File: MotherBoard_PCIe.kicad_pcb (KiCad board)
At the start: 2 copper layers, 91 x 196 mm, 43 parts, among them J1 XT60-M, J10 Bus_mechaken_PCIexpress_x16_1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, J11 Conn_01x03, J12 Conn_01x03, J13 Conn_01x03, J2 XT60-F, J3 Conn_01x07, J4 Conn_01x07, J5 Bus_mechaken_PCIexpress_x16_1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, J6 Bus_mechaken_PCIexpress_x16_1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, J7 Bus_mechaken_PCIexpress_x16_1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, J8 Bus_mechaken_PCIexpress_x16_1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, J9 Bus_mechaken_PCIexpress_x16_1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, U1 NJM7812S

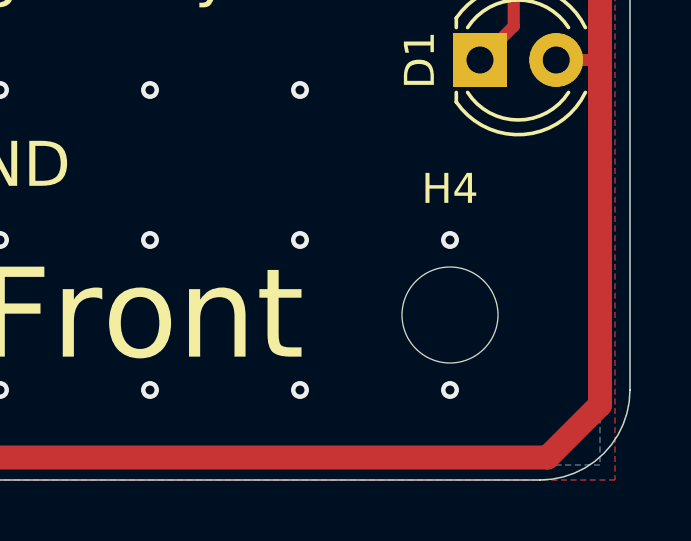
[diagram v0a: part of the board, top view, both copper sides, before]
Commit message: fix
H4にM3ねじを使ったらビアから導通しそうだったので修正
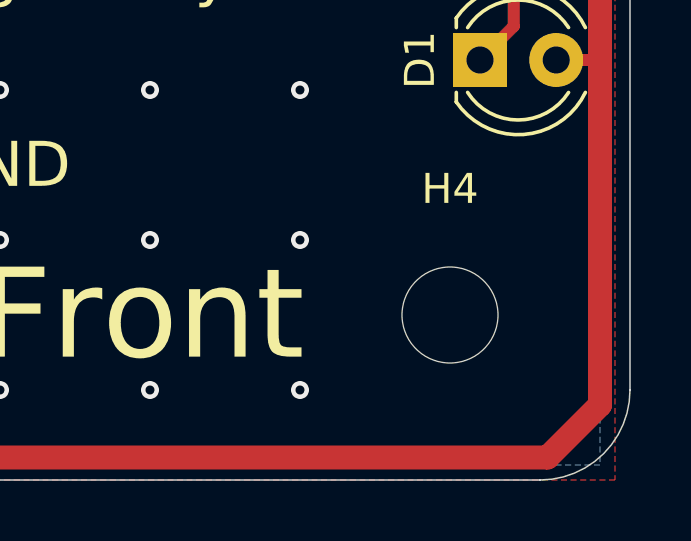
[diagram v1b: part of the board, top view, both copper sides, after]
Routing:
- net GNDPWR: vias 257 -> 255

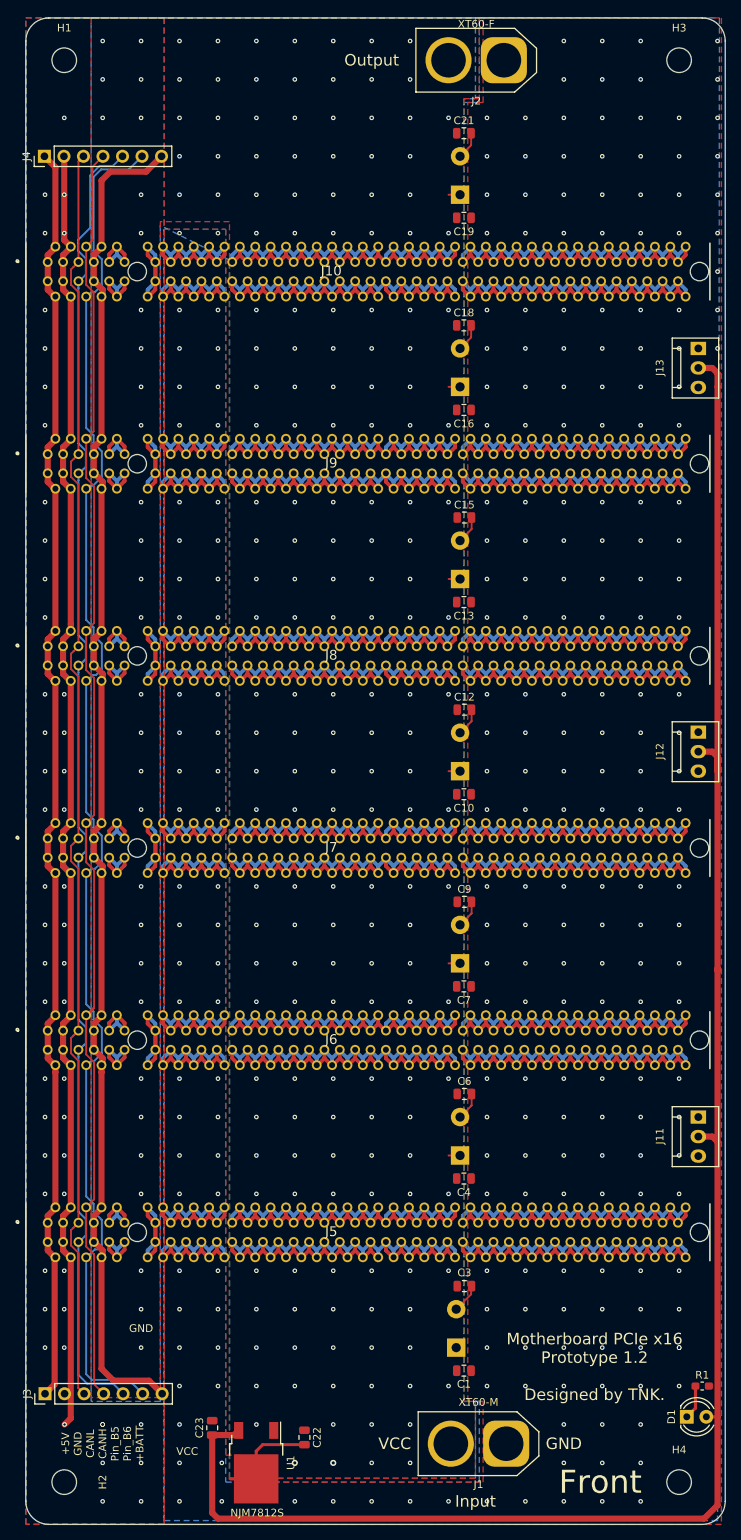
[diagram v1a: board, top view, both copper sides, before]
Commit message: change
シルク印刷の修正（githubのリンク等）
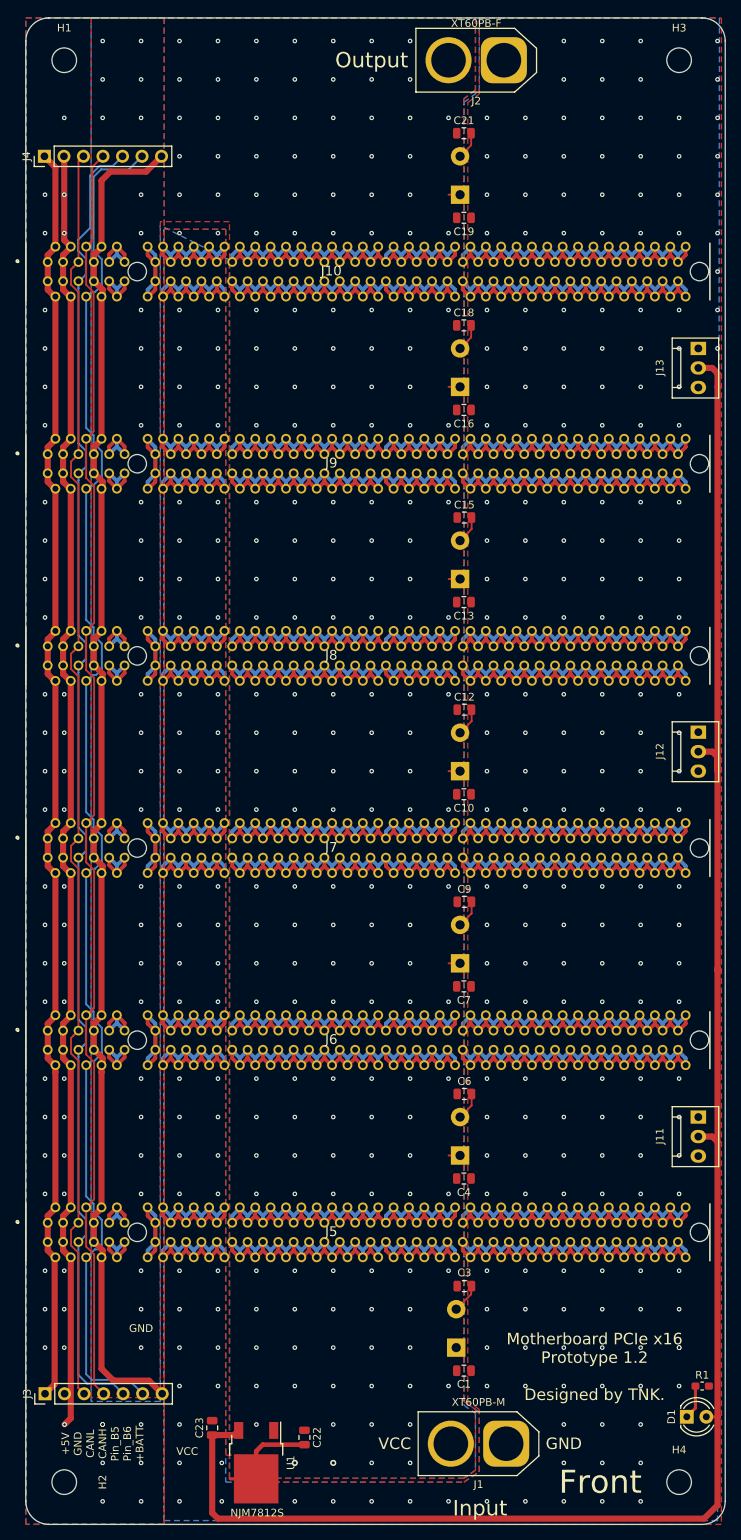
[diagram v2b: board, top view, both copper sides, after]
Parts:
- J1: value XT60-M -> XT60PB-M
- J2: value XT60-F -> XT60PB-F
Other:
- board text added: "https://github.com/picopicodevil/MotherBoard_PCIe.git"
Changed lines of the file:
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@@
   (general
     (thickness 1.6)
-    (drawings 21)
+    (drawings 22)
     (tracks 3433)
     (zones 0)
@@
   )
   (setup
-    (last_trace_width 0.25)
+    (last_trace_width 0.5)
     (user_trace_width 0.2)
     (user_trace_width 0.4)
@@
       (effects (font (size 1 1) (thickness 0.15)))
     )
-    (fp_text value XT60-F (at 3.6 4.7) (layer F.SilkS)
+    (fp_text value XT60PB-F (at 3.6 4.8) (layer F.SilkS)
       (effects (font (size 1 1) (thickness 0.15)))
     )
@@
       (rotate (xyz 0 0 0))
     )
-    (model C:/Users/yuto/OneDrive/Documents/KiCAD/picopicodevil-kicad-library/XT60.pretty/XT60-M--3DModel-STEP-56544.STEP
-      (offset (xyz 3.5 0 16.2))
+    (model "C:/Users/yuto/OneDrive/Documents/KiCAD/picopicodevil-kicad-library/XT60.pretty/XT60 Female Connector.STEP"
+      (offset (xyz 3.5 0 7))
       (scale (xyz 1 1 1))
-      (rotate (xyz 0 0 -90))
+      (rotate (xyz -90 0 0))
     )
   )
@@
       (effects (font (size 1 1) (thickness 0.15)))
     )
-    (fp_text value XT60-M (at 3.6 5.4) (layer F.SilkS)
+    (fp_text value XT60PB-M (at 3.6 5.4) (layer F.SilkS)
       (effects (font (size 1 1) (thickness 0.15)))
     )
@@
       (rotate (xyz 0 0 0))
     )
-    (model C:/Users/yuto/OneDrive/Documents/KiCAD/picopicodevil-kicad-library/XT60.pretty/XT60-M--3DModel-STEP-56544.STEP
-      (offset (xyz 3.5 0 16.2))
+    (model "C:/Users/yuto/OneDrive/Documents/KiCAD/picopicodevil-kicad-library/XT60.pretty/XT60 Male Connector.STEP"
+      (offset (xyz 3.5 0 16))
       (scale (xyz 1 1 1))
-      (rotate (xyz 0 0 -90))
+      (rotate (xyz 90 0 0))
     )
   )
@@
     )
   )
+  (gr_text https://github.com/picopicodevil/MotherBoard_PCIe.git (at 142.85 191.6) (layer B.SilkS)
+    (effects (font (size 1 1) (thickness 0.15)) (justify mirror))
+  )
   (gr_arc (start 78 190) (end 75 190) (angle -90) (layer Edge.Cuts) (width 0.05))
   (gr_arc (start 163 190) (end 163 193) (angle -90) (layer Edge.Cuts) (width 0.05))
@@
   )
   (gr_text "Motherboard PCIe x16\nPrototype 1.2\n\nDesigned by TNK." (at 149 172.5) (layer F.SilkS)
-    (effects (font (size 1.5 1.5) (thickness 0.15)))
+    (effects (font (size 1.5 1.5) (thickness 0.225)))
   )
   (gr_text GND (at 90 167.5) (layer F.SilkS)
@@
   )
   (gr_text GND (at 145 182.5) (layer F.SilkS)
-    (effects (font (size 1.5 1.5) (thickness 0.15)))
+    (effects (font (size 1.5 1.5) (thickness 0.225)))
   )
   (gr_text VCC (at 123 182.5) (layer F.SilkS)
-    (effects (font (size 1.5 1.5) (thickness 0.15)))
+    (effects (font (size 1.5 1.5) (thickness 0.225)))
   )
   (gr_text Output (at 120 2.5) (layer F.SilkS)
-    (effects (font (size 1.5 1.5) (thickness 0.15)))
+    (effects (font (size 2 2) (thickness 0.3)))
   )
-  (gr_text Input (at 133.5 190) (layer F.SilkS)
-    (effects (font (size 1.5 1.5) (thickness 0.15)))
+  (gr_text Input (at 134.1 190.9) (layer F.SilkS)
+    (effects (font (size 2 2) (thickness 0.3)))
   )
   (gr_text "+5V\nGND\nCANL\nCANH\nPin_B5\nPin_B6\n+BATT" (at 85 182.5 90) (layer F.SilkS)
@@
   (segment (start 133 63.5) (end 133 62) (width 0.25) (layer F.Cu) (net 2) (status 20))
   (segment (start 131.5 65) (end 133 63.5) (width 0.25) (layer F.Cu) (net 2) (status 10))
-  (segment (start 104.975 183.475) (end 104.975 187.075) (width 0.4) (layer F.Cu) (net 2) (status 20))
-  (segment (start 105.825 182.625) (end 104.975 183.475) (width 0.4) (layer F.Cu) (net 2))
-  (segment (start 111.25 182.625) (end 105.825 182.625) (width 0.4) (layer F.Cu) (net 2) (status 10))
+  (segment (start 104.975 183.475) (end 104.975 187.075) (width 0.6) (layer F.Cu) (net 2) (status 20))
+  (segment (start 105.825 182.625) (end 104.975 183.475) (width 0.6) (layer F.Cu) (net 2))
+  (segment (start 111.25 182.625) (end 105.825 182.625) (width 0.6) (layer F.Cu) (net 2) (status 10))
   (segment (start 104.975 187.075) (end 101.575 187.075) (width 0.4) (layer F.Cu) (net 2) (status 10))
   (via (at 95 185) (size 0.6) (drill 0.3) (layers F.Cu B.Cu) (net 2))
@@
       (pts
         (xy 165.5 193) (xy 93 193) (xy 93 24.5) (xy 101 24.5) (xy 101 184)
-        (xy 103.5 184) (xy 103.5 187.5) (xy 134.5 187.5) (xy 134.5 177) (xy 132.5 177)
-        (xy 132.5 8) (xy 134.5 8) (xy 134.5 -3) (xy 165.5 -3)
+        (xy 103.5 184) (xy 103.5 187.5) (xy 132 187.5) (xy 134 186.15) (xy 134 178.05)
+        (xy 132.5 177) (xy 132.5 8) (xy 134 6.9) (xy 134 -3) (xy 165.5 -3)
       )
     )
@@
     (polygon
       (pts
-        (xy 134 7.5) (xy 132 7.5) (xy 132 177) (xy 133.5 177) (xy 133.5 187)
-        (xy 101.5 187) (xy 101.5 23.5) (xy 92.5 23.5) (xy 92.5 176.5) (xy 83.5 176.5)
-        (xy 83.5 -3) (xy 134 -3)
+        (xy 133.5 6.4) (xy 132 7.5) (xy 132 177) (xy 133.5 178.05) (xy 133.5 185.95)
+        (xy 132 187) (xy 101.5 187) (xy 101.5 23.5) (xy 92.5 23.5) (xy 92.5 176.5)
+        (xy 83.5 176.5) (xy 83.5 -3) (xy 133.5 -3)
       )
     )
@@
       (pts
         (xy 165 192.5) (xy 93 192.5) (xy 93 24.5) (xy 101 24.5) (xy 101 187.5)
-        (xy 134 187.5) (xy 134.012973 177) (xy 132 177) (xy 132 8) (xy 134 7.998589)
-        (xy 134 -3) (xy 165.25 -3)
+        (xy 132 187.5) (xy 134 186.15) (xy 134 178.4) (xy 132 177) (xy 132 8)
+        (xy 134 6.5) (xy 134 -3) (xy 165.25 -3)
       )
     )
@@
     (polygon
       (pts
-        (xy 133.5 7.5) (xy 132 7.5) (xy 132 177.5) (xy 133.5 177.5) (xy 133.5 187)
-        (xy 101.5 187) (xy 101.5 28.5) (xy 92.5 24) (xy 92.5 177) (xy 83.5 177)
-        (xy 83.5 -3) (xy 133.5 -3)
+        (xy 133.5 6.4) (xy 132 7.5) (xy 132 177.5) (xy 133.5 178.55) (xy 133.5 185.95)
+        (xy 132 187) (xy 101.5 187) (xy 101.5 28.5) (xy 92.5 24) (xy 92.5 177)
+        (xy 83.5 177) (xy 83.5 -3) (xy 133.5 -3)
       )
     )
